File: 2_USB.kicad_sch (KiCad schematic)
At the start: 7 parts, among them J301 USB_C_Receptacle_USB2.0_16P, U301 USBLC6-2SC6, U302 CH224K, U303 USBLC6-2SC6

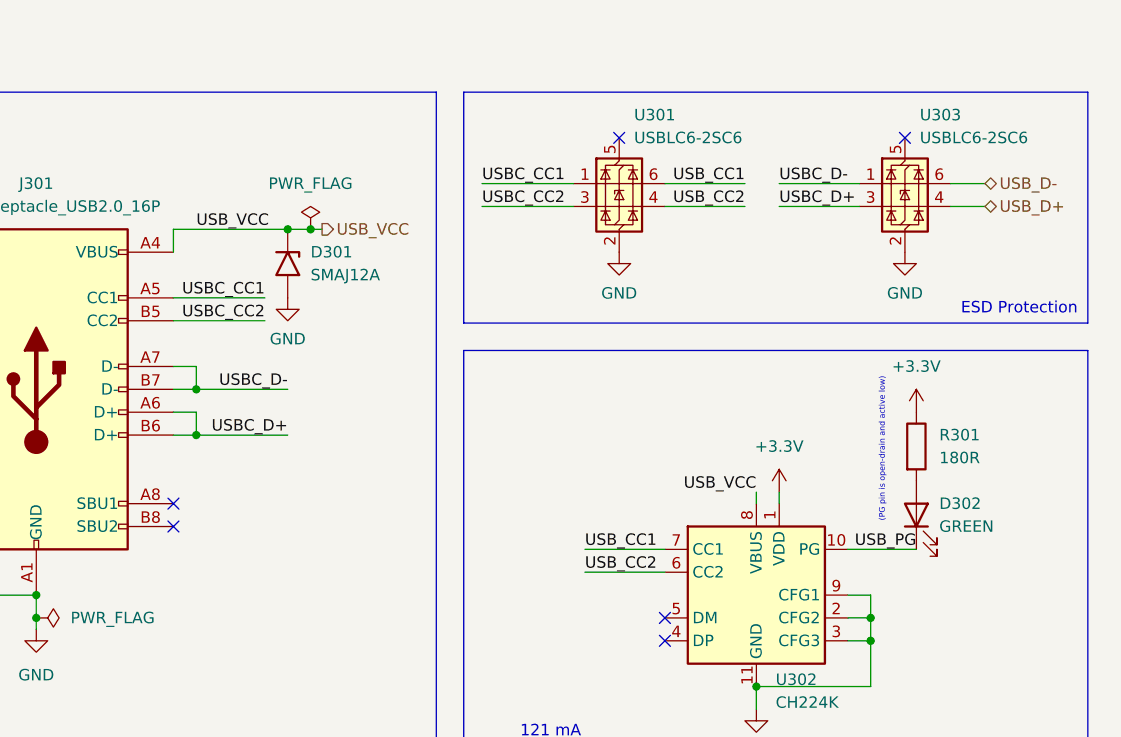
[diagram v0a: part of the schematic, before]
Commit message: Major changes
Updated schematic for better power delivery
Changed 3.3V supply to buck converter instead of LDO due to heat
Deleted the entire PCB, redoing the whole thing due to problems in
laying traces that made some connections impossible to make
Also updated README to reflect these changes
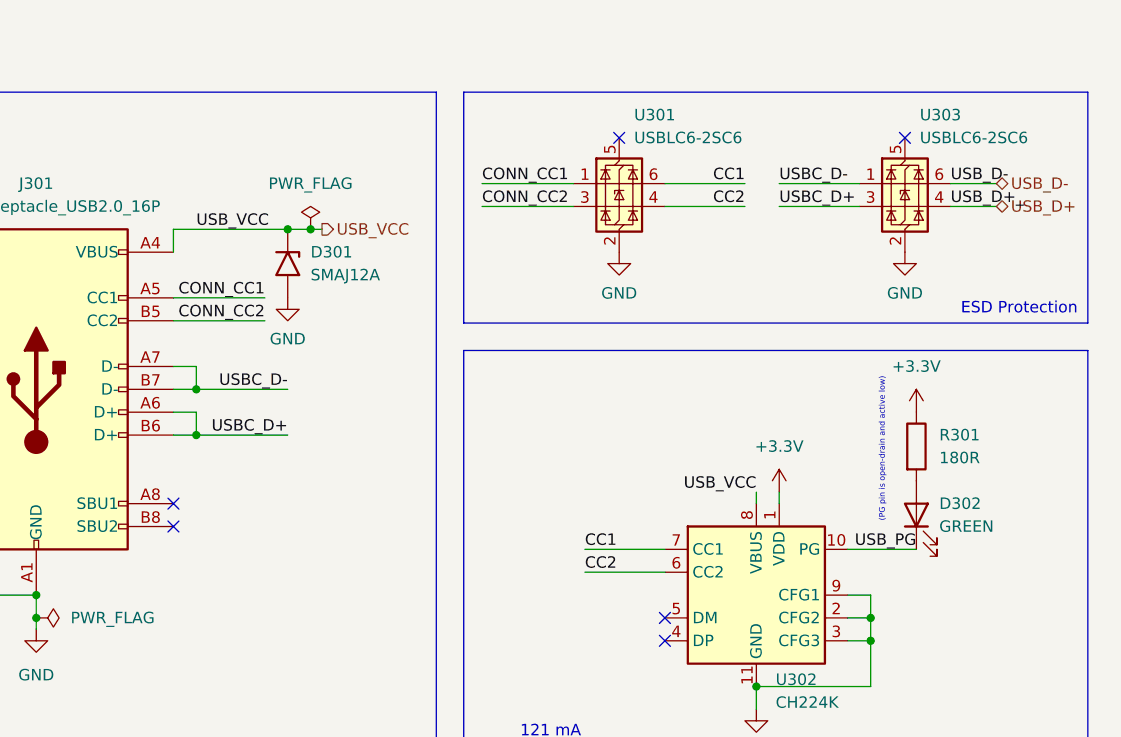
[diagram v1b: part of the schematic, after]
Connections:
- net USBC_CC1 renamed CONN_CC1
- net USBC_CC2 renamed CONN_CC2
- net USB_CC1 renamed CC1
- net USB_CC2 renamed CC2
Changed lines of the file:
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@@
 	(wire
 		(pts
-			(xy 187.96 74.93) (xy 191.77 74.93)
+			(xy 187.96 74.93) (xy 193.04 74.93)
 		)
 		(stroke
@@
 	(wire
 		(pts
-			(xy 187.96 72.39) (xy 191.77 72.39)
+			(xy 187.96 72.39) (xy 193.04 72.39)
 		)
 		(stroke
@@
 			(width 0)
 			(type default)
+		)
+	)
+	(label "USB_D+_"
+		(at 187.96 74.93 0)
+		(effects
+			(font
+				(size 1.27 1.27)
+			)
+			(justify left bottom)
 		)
 	)
@@
 		)
 	)
-	(label "USBC_CC2"
+	(label "CONN_CC2"
 		(at 135.89 74.93 0)
 		(effects
@@
 		)
 	)
-	(label "USB_CC2"
+	(label "CC2"
 		(at 165.1 74.93 180)
 		(effects
@@
 		)
 	)
-	(label "USBC_CC1"
+	(label "CONN_CC1"
 		(at 111.76 85.09 180)
 		(effects
@@
 		)
 	)
-	(label "USBC_CC2"
+	(label "USB_D-"
+		(at 187.96 72.39 0)
+		(effects
+			(font
+				(size 1.27 1.27)
+			)
+			(justify left bottom)
+		)
+	)
+	(label "CONN_CC2"
 		(at 111.76 87.63 180)
 		(effects
@@
 		)
 	)
-	(label "USBC_CC1"
+	(label "CONN_CC1"
 		(at 135.89 72.39 0)
 		(effects
@@
 		)
 	)
-	(label "USB_CC1"
+	(label "CC1"
 		(at 147.32 113.03 0)
 		(effects
@@
 		)
 	)
-	(label "USB_CC2"
+	(label "CC2"
 		(at 147.32 115.57 0)
 		(effects
@@
 		)
 	)
-	(label "USB_CC1"
+	(label "CC1"
 		(at 165.1 72.39 180)
 		(effects
@@
 	(hierarchical_label "USB_D-"
 		(shape bidirectional)
-		(at 191.77 72.39 0)
+		(at 193.04 72.39 0)
 		(effects
 			(font
@@
 	(hierarchical_label "USB_D+"
 		(shape bidirectional)
-		(at 191.77 74.93 0)
-		(effects
-			(font
+		(at 193.04 74.93 0)
+		(effects
+			(font

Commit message: Finished most of component re-placement
Began laying tracks for important connections
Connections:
- net CC1: now also U301.4 (I/O2); no longer U301.6 (I/O1)
- net CC2: now also U301.6 (I/O1); no longer U301.4 (I/O2)
- net CONN_CC1: now also U301.3 (I/O2); no longer U301.1 (I/O1)
- net CONN_CC2: now also U301.1 (I/O1); no longer U301.3 (I/O2)
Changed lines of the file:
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@@
 		)
 	)
-	(label "USB_D+_"
+	(label "USB_D+"
 		(at 187.96 74.93 0)
 		(effects
@@
 	)
 	(label "CONN_CC2"
-		(at 135.89 74.93 0)
+		(at 135.89 72.39 0)
 		(effects
 			(font
@@
 	)
 	(label "CC2"
-		(at 165.1 74.93 180)
+		(at 165.1 72.39 180)
 		(effects
 			(font
@@
 	)
 	(label "CONN_CC1"
-		(at 135.89 72.39 0)
+		(at 135.89 74.93 0)
 		(effects
 			(font
@@
 	)
 	(label "CC1"
-		(at 165.1 72.39 180)
-		(effects
-			(font
+		(at 165.1 74.93 180)
+		(effects
+			(font
